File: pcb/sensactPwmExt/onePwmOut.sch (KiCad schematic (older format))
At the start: 4 parts, among them P3 CONN_01X02, U2 LED_DRIVER

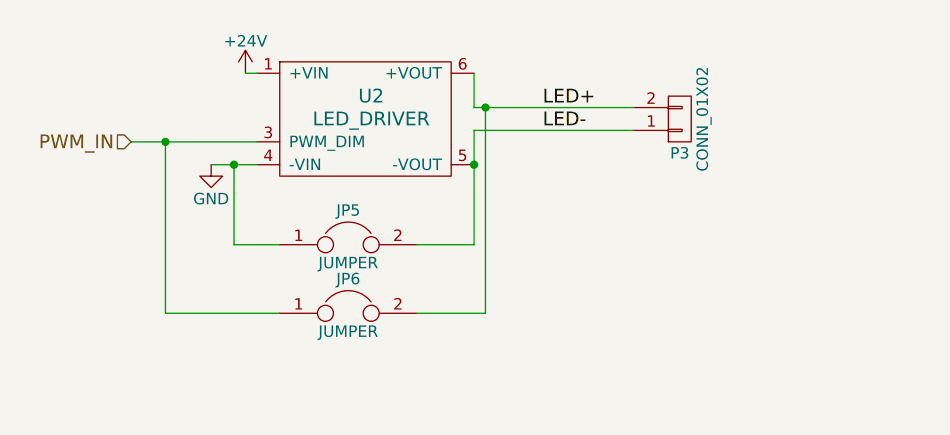
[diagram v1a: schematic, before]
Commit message: Redesign sensactInpExt
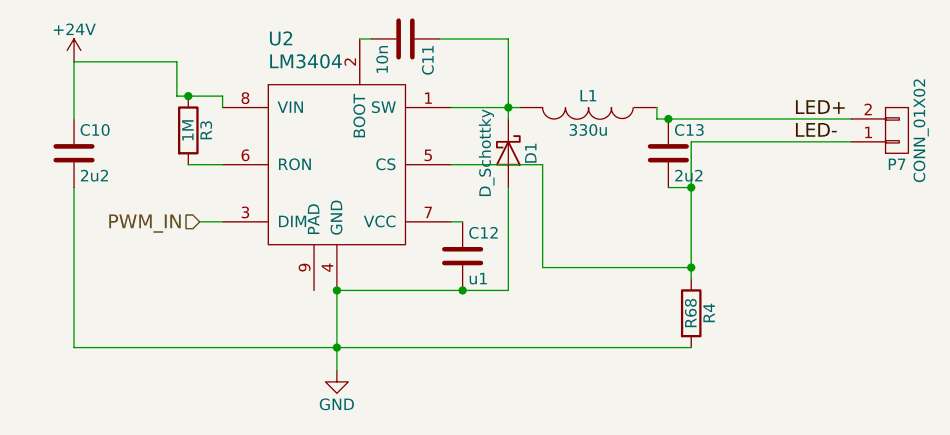
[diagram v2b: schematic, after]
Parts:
- removed JP5, JP6: JUMPER, Resistors_SMD:R_0603, symbol JUMPER
- removed U2: LED_DRIVER, sensact:MEANWELL_LDD_L, symbol LED_DRIVER
- added C70, C73: 2u2, Resistors_SMD:R_1210_HandSoldering, symbol C
- added C71: 10n, Resistors_SMD:R_0805_HandSoldering, symbol C
- added C72: u1, Resistors_SMD:R_0805_HandSoldering, symbol C
- added D16: D_Schottky, sensact:do214ac_handsolder, symbol D_Schottky
- added L16: 330u, sensact:CD127, symbol INDUCTOR
- added R33: 1M, Resistors_SMD:R_0805_HandSoldering, symbol R
- added R34: R68, Resistors_SMD:R_1206_HandSoldering, symbol R
- added U17: LM3404, sensact:SOIC-8_3.9x4.9mm_Pitch1.27mm_handsolder, symbol LM3404
- renumbered P3 to P22
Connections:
- net +24V: now also C70.1, R33.1, U17.8 (VIN)
- net GND: now also C70.2, C72.2, D16.2 (A), R34.2, U17.4 (GND)
- net LED+: now also C73.1, L16.1
- net LED-: now also C73.2, R34.1, U17.5 (CS)
- net PWM_IN: now also U17.3 (DIM)
- new net: C71.1, D16.1 (K), L16.2, U17.1 (SW)
- new net: C71.2, U17.2 (BOOT)
- new net: R33.2, U17.6 (RON)
- new net: C72.1, U17.7 (VCC)
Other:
- moved on the sheet: P7

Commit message: pwmext completed and basically ready for ordering
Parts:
- U17: footprint sensact:SOIC-8_3.9x4.9mm_Pitch1.27mm_handsolder -> sensact:SOIC-8_3.9x4.9mm_Pitch1.27mm_pad_handsolder
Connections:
- net GND: now also U17.9 (PAD)
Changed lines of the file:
@@
 $Descr A4 11693 8268
 encoding utf-8
-Sheet 17 9
+Sheet 4 9
 Title ""
 Date ""
@@
 P 5750 4450
 AR Path="/57CDCEC1/57CCF171" Ref="#PWR049"  Part="1"
-AR Path="/57CCF017/57CCF171" Ref="#PWR019"  Part="1"
-AR Path="/57CD0726/57CCF171" Ref="#PWR021"  Part="1"
-AR Path="/57CD07F6/57CCF171" Ref="#PWR023"  Part="1"
-AR Path="/57CD080D/57CCF171" Ref="#PWR025"  Part="1"
-AR Path="/57CD0824/57CCF171" Ref="#PWR027"  Part="1"
-AR Path="/57CD083B/57CCF171" Ref="#PWR029"  Part="1"
-AR Path="/57CD0852/57CCF171" Ref="#PWR031"  Part="1"
-AR Path="/57CD0869/57CCF171" Ref="#PWR033"  Part="1"
+AR Path="/57CCF017/57CCF171" Ref="#PWR024"  Part="1"
+AR Path="/57CD0726/57CCF171" Ref="#PWR026"  Part="1"
+AR Path="/57CD07F6/57CCF171" Ref="#PWR028"  Part="1"
+AR Path="/57CD080D/57CCF171" Ref="#PWR030"  Part="1"
+AR Path="/57CD0824/57CCF171" Ref="#PWR032"  Part="1"
+AR Path="/57CD083B/57CCF171" Ref="#PWR034"  Part="1"
+AR Path="/57CD0852/57CCF171" Ref="#PWR036"  Part="1"
+AR Path="/57CD0869/57CCF171" Ref="#PWR038"  Part="1"
 AR Path="/57CDCD72/57CCF171" Ref="#PWR035"  Part="1"
 AR Path="/57CDCD9C/57CCF171" Ref="#PWR037"  Part="1"
@@
 AR Path="/57CDCE6B/57CCF171" Ref="#PWR045"  Part="1"
 AR Path="/57CDCE97/57CCF171" Ref="#PWR047"  Part="1"
-F 0 "#PWR033" H 5750 4200 50  0001 C CNN
+F 0 "#PWR024" H 5750 4200 50  0001 C CNN
 F 1 "GND" H 5750 4300 50  0000 C CNN
 F 2 "" H 5750 4450 50  0000 C CNN
@@
 P 4600 3100
 AR Path="/57CDCEC1/57CCF189" Ref="#PWR050"  Part="1"
-AR Path="/57CCF017/57CCF189" Ref="#PWR020"  Part="1"
-AR Path="/57CD0726/57CCF189" Ref="#PWR022"  Part="1"
-AR Path="/57CD07F6/57CCF189" Ref="#PWR024"  Part="1"
-AR Path="/57CD080D/57CCF189" Ref="#PWR026"  Part="1"
-AR Path="/57CD0824/57CCF189" Ref="#PWR028"  Part="1"
-AR Path="/57CD083B/57CCF189" Ref="#PWR030"  Part="1"
-AR Path="/57CD0852/57CCF189" Ref="#PWR032"  Part="1"
-AR Path="/57CD0869/57CCF189" Ref="#PWR034"  Part="1"
+AR Path="/57CCF017/57CCF189" Ref="#PWR025"  Part="1"
+AR Path="/57CD0726/57CCF189" Ref="#PWR027"  Part="1"
+AR Path="/57CD07F6/57CCF189" Ref="#PWR029"  Part="1"
+AR Path="/57CD080D/57CCF189" Ref="#PWR031"  Part="1"
+AR Path="/57CD0824/57CCF189" Ref="#PWR033"  Part="1"
+AR Path="/57CD083B/57CCF189" Ref="#PWR035"  Part="1"
+AR Path="/57CD0852/57CCF189" Ref="#PWR037"  Part="1"
+AR Path="/57CD0869/57CCF189" Ref="#PWR039"  Part="1"
 AR Path="/57CDCD72/57CCF189" Ref="#PWR036"  Part="1"
 AR Path="/57CDCD9C/57CCF189" Ref="#PWR038"  Part="1"
@@
 AR Path="/57CDCE6B/57CCF189" Ref="#PWR046"  Part="1"
 AR Path="/57CDCE97/57CCF189" Ref="#PWR048"  Part="1"
-F 0 "#PWR034" H 4600 2950 50  0001 C CNN
+F 0 "#PWR025" H 4600 2950 50  0001 C CNN
 F 1 "+24V" H 4600 3240 50  0000 C CNN
 F 2 "" H 4600 3100 50  0000 C CNN
@@
 F 0 "U2" H 5450 4400 60  0000 L CNN
 F 1 "LM3404" H 5450 4300 60  0000 L CNN
-F 2 "sensact:SOIC-8_3.9x4.9mm_Pitch1.27mm_handsolder" H 5800 3700 60  0001 C CNN
+F 2 "sensact:SOIC-8_3.9x4.9mm_Pitch1.27mm_pad_handsolder" H 5800 3700 60  0001 C CNN
 F 3 "" H 5800 3700 60  0001 C CNN
 	1    5750 3700
@@
 Wire Wire Line
 	5900 3000 5850 3000
+Wire Wire Line
+	5650 4100 5650 4350
+Connection ~ 5650 4350
 $EndSCHEMATC
